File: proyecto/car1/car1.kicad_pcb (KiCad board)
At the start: 2 copper layers, 137 x 85.9 mm, 30 parts, among them J1 HC-sr04, J10 vcc Edu ciaa, J11 Adafruit A, J12 Adafruit B, J2 HC-sr04, J3 HC-sr04, J4 usb c socket, J5 SERVO, J6 Conn_01x08_Socket, J7 Conn_01x08_Socket, J8 Conn_01x19, J9 Conn_01x19

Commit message: arreglos menores
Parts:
- removed MP?: Plantilla_EDU-CIAA, Poncho_Esqueleto:Plantilla_EDU-CIAA

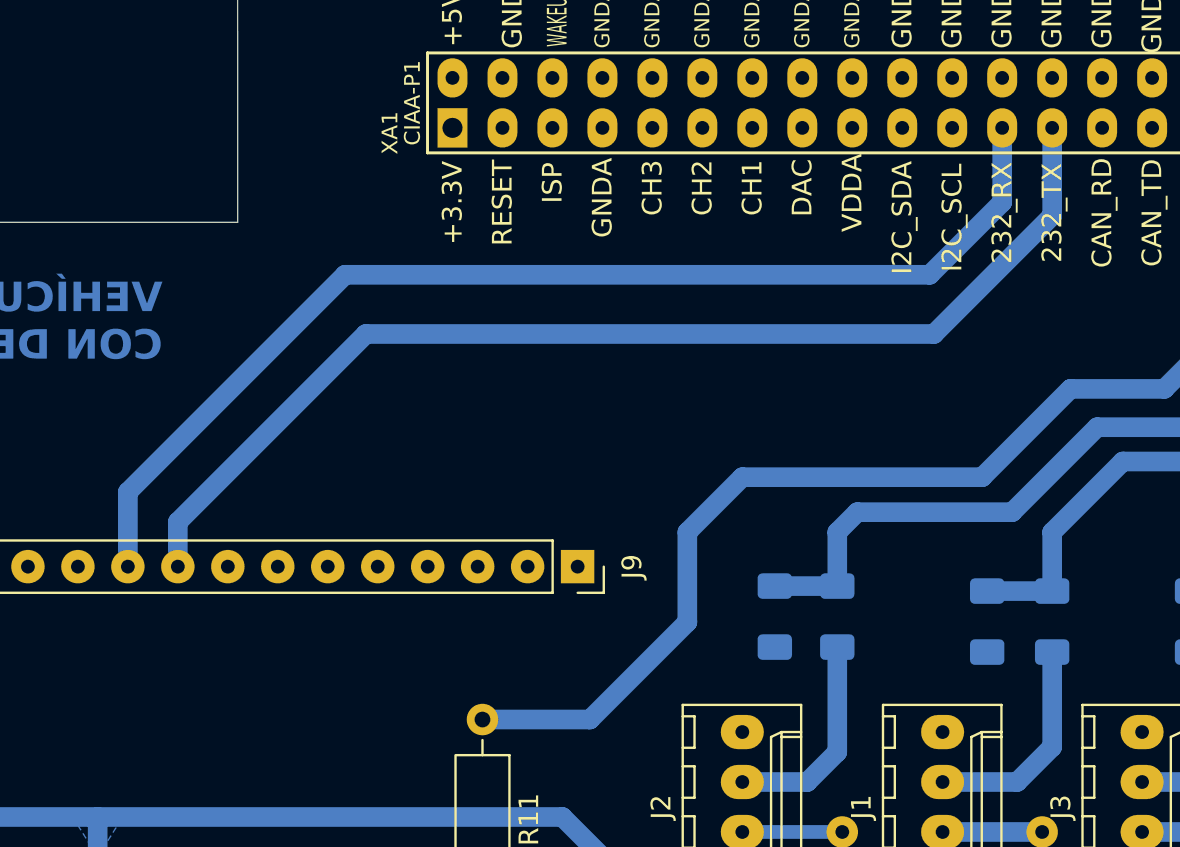
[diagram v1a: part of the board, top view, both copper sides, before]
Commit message: fix esp32
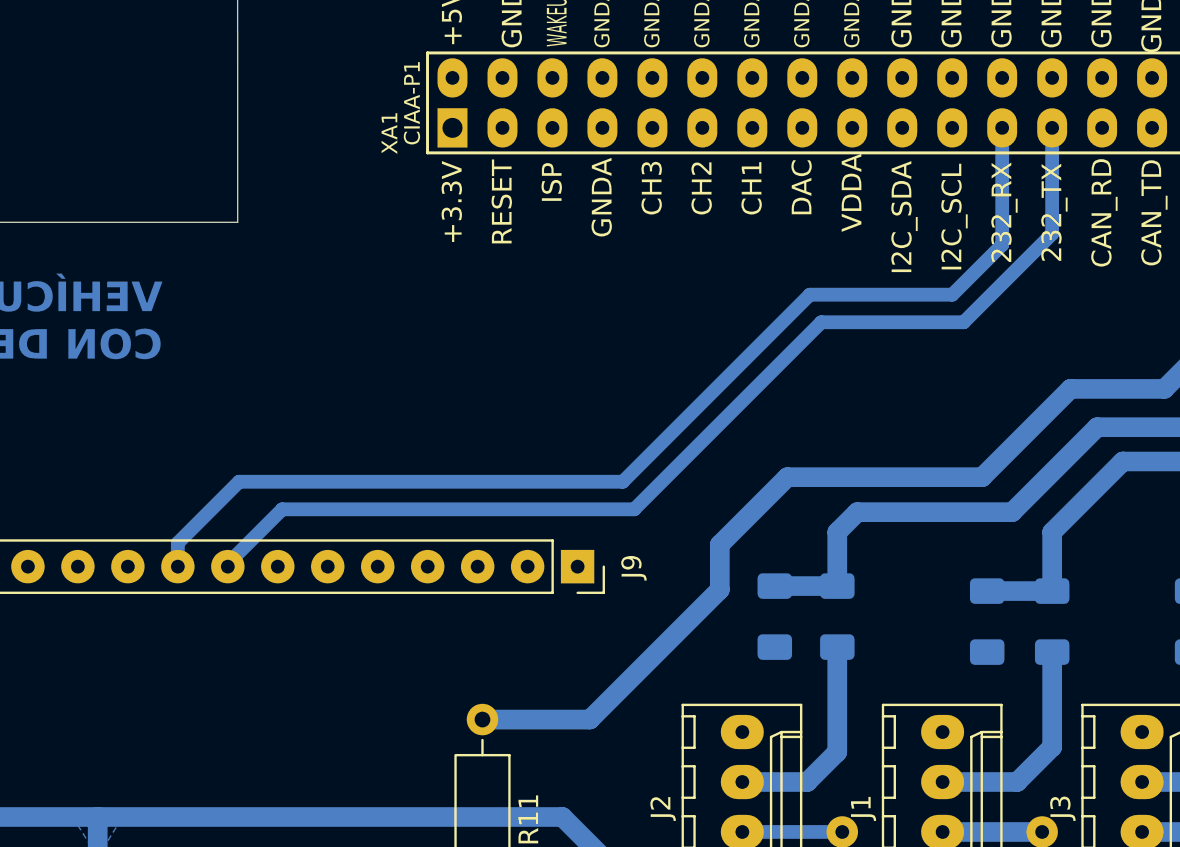
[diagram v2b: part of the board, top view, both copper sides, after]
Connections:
- J8 pad 14: unconnected-(J8-Pin_14-Pad14) -> GND
- J9 pad 10: D7  RS232_RX -> unconnected-(J9-Pin_10-Pad10)
- J9 pad 19: unconnected-(J9-Pin_19-Pad19) -> GND
- J9 pad 7: GND -> unconnected-(J9-Pin_7-Pad7)
- J9 pad 8: unconnected-(J9-Pin_8-Pad8) -> RS232_TX
- J9 pad 9: D6  RS232_TX -> RS232_RX
- XA1 pad 23: D7  RS232_RX -> RS232_RX
- XA1 pad 25: D6  RS232_TX -> RS232_TX
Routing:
- net D7  RS232_RX: track 58.1 -> 0.00 mm
- net D6  RS232_TX: track 57.6 -> 0.00 mm
- net RS232_RX: track 0.00 -> 55.3 mm
- net RS232_TX: track 0.00 -> 54.4 mm
- net Net-(XA1A-tecCOL1): track 58.4 -> 57.0 mm
